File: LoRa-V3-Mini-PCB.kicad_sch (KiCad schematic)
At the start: 23 parts, among them Q1 SI2367DS-T1-GE3, SW1 434331045822, SW2 434331045816, U1 114993121, U2 BR24G1MFVT, U3 SHT40, U4 TSL25911

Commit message: move global components into project library
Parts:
- C1, C10, C11, C2, C3, C5: footprint 1GlobalFootprintsLibrary:C_0603_nominal -> 1projectLibrary:C_0603_nominal
- R1, R2, R3, R4: footprint 1GlobalFootprintsLibrary:R_0603_nominal -> 1projectLibrary:R_0603_nominal
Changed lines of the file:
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@@
 			)
 		)
-		(property "Footprint" "1GlobalFootprintsLibrary:C_0603_nominal"
+		(property "Footprint" "1projectLibrary:C_0603_nominal"
 			(at 35.8648 101.6 0)
 			(effects
@@
 			)
 		)
-		(property "Footprint" "1GlobalFootprintsLibrary:C_0603_nominal"
+		(property "Footprint" "1projectLibrary:C_0603_nominal"
 			(at 55.5752 101.6 0)
 			(effects
@@
 			)
 		)
-		(property "Footprint" "1GlobalFootprintsLibrary:R_0603_nominal"
+		(property "Footprint" "1projectLibrary:R_0603_nominal"
 			(at 96.012 54.61 90)
 			(effects
@@
 			)
 		)
-		(property "Footprint" "1GlobalFootprintsLibrary:R_0603_nominal"
+		(property "Footprint" "1projectLibrary:R_0603_nominal"
 			(at 129.032 73.66 90)
 			(effects
@@
 			)
 		)
-		(property "Footprint" "1GlobalFootprintsLibrary:C_0603_nominal"
+		(property "Footprint" "1projectLibrary:C_0603_nominal"
 			(at 247.3452 62.23 0)
 			(effects
@@
 			)
 		)
-		(property "Footprint" "1GlobalFootprintsLibrary:R_0603_nominal"
+		(property "Footprint" "1projectLibrary:R_0603_nominal"
 			(at 134.112 73.66 90)
 			(effects
@@
 			)
 		)
-		(property "Footprint" "1GlobalFootprintsLibrary:C_0603_nominal"
+		(property "Footprint" "1projectLibrary:C_0603_nominal"
 			(at 46.6852 101.6 0)
 			(effects
@@
 			)
 		)
-		(property "Footprint" "1GlobalFootprintsLibrary:C_0603_nominal"
+		(property "Footprint" "1projectLibrary:C_0603_nominal"
 			(at 253.6952 62.23 0)
 			(effects
@@
 			)
 		)
-		(property "Footprint" "1GlobalFootprintsLibrary:C_0603_nominal"
+		(property "Footprint" "1projectLibrary:C_0603_nominal"
 			(at 265.1252 147.32 0)
 			(effects
@@
 			)
 		)
-		(property "Footprint" "1GlobalFootprintsLibrary:R_0603_nominal"
+		(property "Footprint" "1projectLibrary:R_0603_nominal"
 			(at 139.192 73.66 90)
 			(effects

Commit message: update 3d models / footprints
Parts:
- U1: footprint 1GlobalFootprintsLibrary:LoRa-E5 -> 1projectLibrary:LoRa-E5
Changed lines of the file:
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@@
 			)
 		)
-		(property "Footprint" "1GlobalFootprintsLibrary:LoRa-E5"
+		(property "Footprint" "1projectLibrary:LoRa-E5"
 			(at 233.68 106.68 0)
 			(effects

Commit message: using project lib io global
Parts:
- F1, F2, F3: footprint Fiducial:Fiducial_0.75mm_Mask1.5mm -> Fiducial:Fiducial_0.5mm_Mask1mm
- U3: footprint 1GlobalFootprintsLibrary:SHT4X -> 1projectLibrary:SHT4X
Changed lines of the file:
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@@
 			)
 		)
-		(property "Footprint" "Fiducial:Fiducial_0.75mm_Mask1.5mm"
+		(property "Footprint" "Fiducial:Fiducial_0.5mm_Mask1mm"
 			(at 167.64 180.34 0)
 			(effects
@@
 			)
 		)
-		(property "Footprint" "Fiducial:Fiducial_0.75mm_Mask1.5mm"
+		(property "Footprint" "Fiducial:Fiducial_0.5mm_Mask1mm"
 			(at 167.64 175.26 0)
 			(effects
@@
 			)
 		)
-		(property "Footprint" "Fiducial:Fiducial_0.75mm_Mask1.5mm"
+		(property "Footprint" "Fiducial:Fiducial_0.5mm_Mask1mm"
 			(at 167.64 185.42 0)
 			(effects
@@
 			)
 		)
-		(property "Footprint" "1GlobalFootprintsLibrary:SHT4X"
+		(property "Footprint" "1projectLibrary:SHT4X"
 			(at 68.58 128.27 0)
 			(effects
@@
 			)
 		)
-		(property "Description" "SHT40"
+		(property "Description" "Digital Relative Humidity Temperature Sensor"
 			(at 69.85 110.49 0)
 			(effects

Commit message: update libraries
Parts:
- ANT1: footprint 1GlobalFootprintsLibrary:XDCR_ANT-868-CHP-T -> 1projectLibrary:XDCR_ANT-868-CHP-T
- SW1: manufacturerPartNumber 434331045822 -> 434133025816
- SW2: footprint 1GlobalFootprintsLibrary:4341330258X6 -> 1projectLibrary:4341330258X6; GPN (none) -> NA
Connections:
- net GND: now also SW1.2; no longer SW1.3
- net SWO: now also SW1.3; no longer SW1.2
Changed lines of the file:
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@@
 			)
 		)
-		(property "Datasheet" "https://www.we-online.com/katalog/datasheet/434331045822.pdf"
+		(property "Datasheet" "https://www.we-online.com/components/products/datasheet/434133025816.pdf"
 			(at 205.994 89.662 0)
 			(effects
@@
 			)
 		)
-		(property "Description" "ApplicationButton"
+		(property "Description" "Application buttonswitch"
 			(at 194.31 94.488 0)
 			(effects
@@
 			)
 		)
-		(property "manufacturerPartNumber" "434331045822"
+		(property "manufacturerPartNumber" "434133025816"
 			(at 207.01 87.63 0)
 			(effects
@@
 			)
 		)
-		(property "Footprint" "1GlobalFootprintsLibrary:XDCR_ANT-868-CHP-T"
+		(property "Footprint" "1projectLibrary:XDCR_ANT-868-CHP-T"
 			(at 207.01 132.715 0)
 			(effects
@@
 			)
 		)
-		(property "Footprint" "1GlobalFootprintsLibrary:4341330258X6"
+		(property "Footprint" "1projectLibrary:4341330258X6"
 			(at 254.762 126.746 0)
 			(effects
@@
 			(at 254 143.51 0)
 			(effects
+				(font
+					(size 1.27 1.27)
+				)
+				(hide yes)
+			)
+		)
+		(property "GPN" "NA"
+			(at 254 143.51 0)
+			(effects

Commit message: update application switch
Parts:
- SW1: symbol 1GlobalSymbolsLibrary:Switch_434331045822 -> 1projectLibrary:Switch_434331045822
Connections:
- net GND: now also SW1.3; no longer SW1.2
- net SWO: now also SW1.2; no longer SW1.3
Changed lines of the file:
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@@
 	)
 	(symbol
-		(lib_id "1GlobalSymbolsLibrary:Switch_434331045822")
+		(lib_id "1projectLibrary:Switch_434331045822")
 		(at 207.01 95.25 180)
 		(unit 1)
@@
 			)
 		)
-		(property "Datasheet" "https://www.we-online.com/components/products/datasheet/434133025816.pdf"
+		(property "Datasheet" "https://www.we-online.com/katalog/datasheet/434331045822.pdf"
 			(at 205.994 89.662 0)
 			(effects
@@
 		)
 		(property "Description" "Application buttonswitch"
-			(at 194.31 94.488 0)
+			(at 207.01 74.93 0)
 			(effects
 				(font
 					(size 1.27 1.27)
 				)
+				(hide yes)
 			)
 		)

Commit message: wip
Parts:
- Q1: footprint 1GlobalFootprintsLibrary:SI2367DS-SOT-23 -> 1projectLibrary:SI2367DS-SOT-23; symbol 1GlobalSymbolsLibrary:Si2367DS -> 1projectLibrary:Si2367DS
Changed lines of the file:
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@@
 	)
 	(symbol
-		(lib_id "1GlobalSymbolsLibrary:Si2367DS")
+		(lib_id "1projectLibrary:Si2367DS")
 		(at 90.17 59.69 0)
 		(mirror y)
@@
 			)
 		)
-		(property "Footprint" "1GlobalFootprintsLibrary:SI2367DS-SOT-23"
+		(property "Footprint" "1projectLibrary:SI2367DS-SOT-23"
 			(at 99.568 87.122 0)
 			(effects

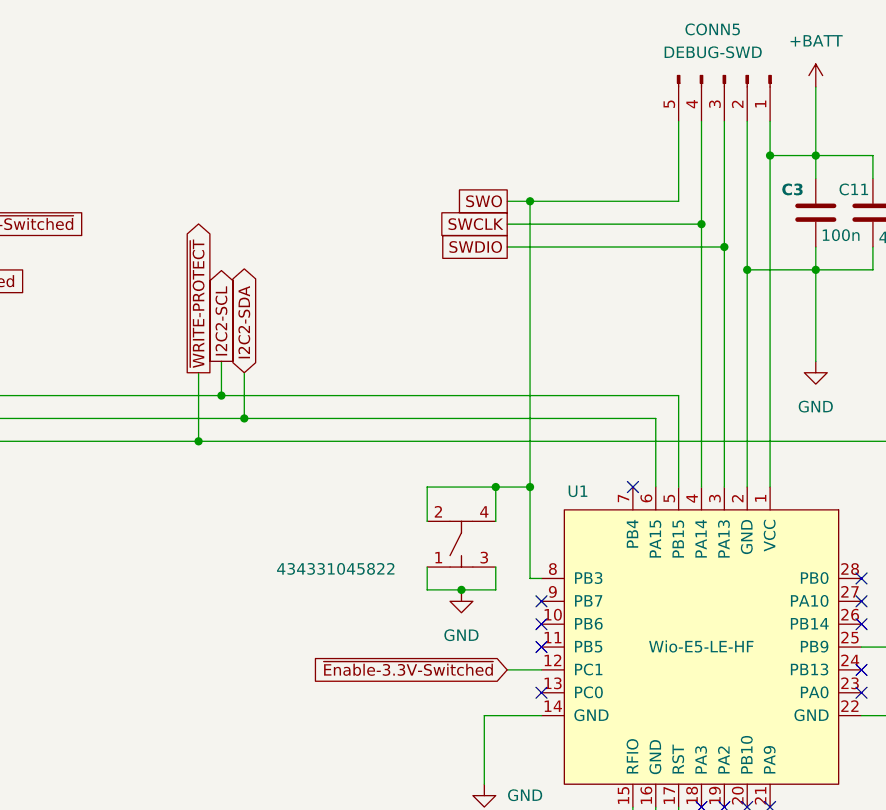
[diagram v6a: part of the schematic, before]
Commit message: upgraded debug connector with UART1TX
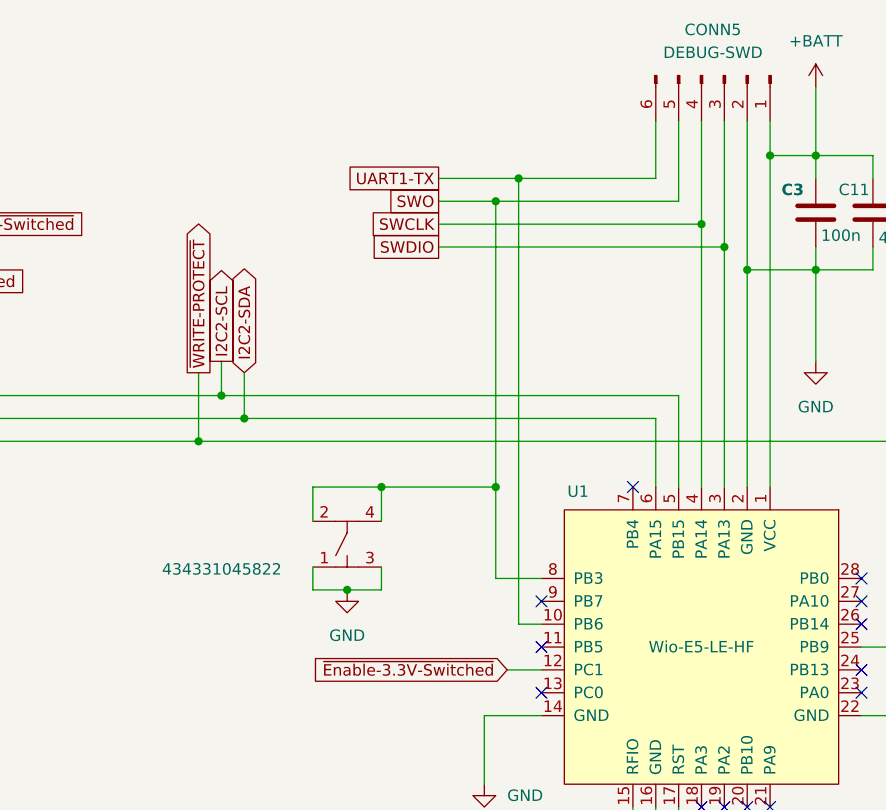
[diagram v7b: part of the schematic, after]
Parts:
- CONN5: footprint 1projectLibrary:PinHeader_1x05_P2.54mm_Vertical -> 1projectLibrary:DebugConnector_1x06_P2.54mm; symbol 1projectLibrary:DebugPortConnector -> 1projectLibrary:DebugConnector-6p
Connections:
- net UART1-TX: now reaches U1.10 (PB6)
- net UART1-TX: now also CONN5.6 (Pin_6)
- no-connect marks 15 -> 14

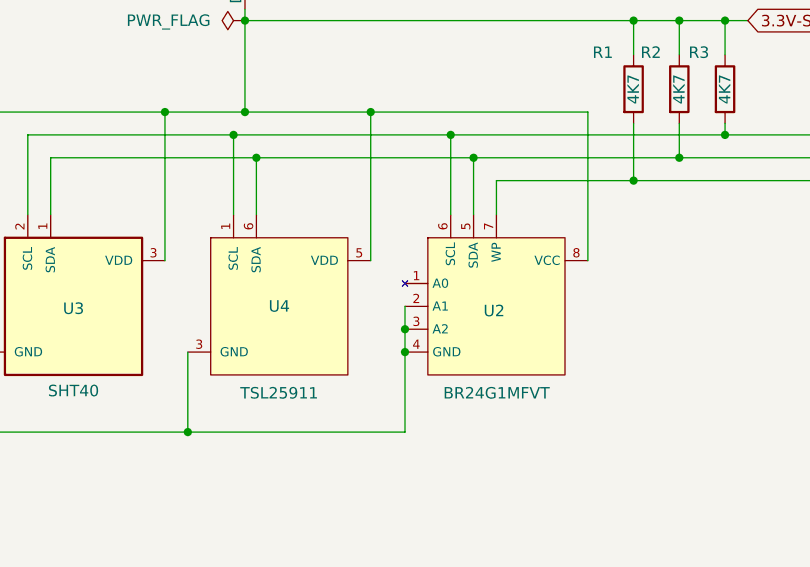
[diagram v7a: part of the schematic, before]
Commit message: fix 3d-models
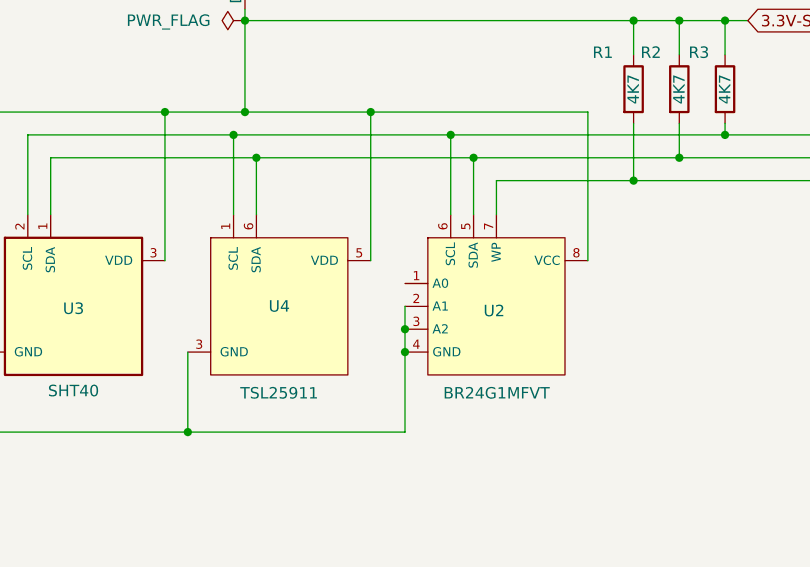
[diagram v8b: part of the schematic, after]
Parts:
- U2: footprint 1GlobalFootprintsLibrary:BR24G1M-TSSOP-B8 -> 1projectLibrary:BR24G1M-TSSOP-B8; symbol 1GlobalSymbolsLibrary:BR24G1MFVT -> 1projectLibrary:BR24G1MFVT
- U4: footprint 1GlobalFootprintsLibrary:TSL2591 -> 1projectLibrary:TSL2591-SON; symbol 1GlobalSymbolsLibrary:TSL2591 -> 1projectLibrary:TSL2591
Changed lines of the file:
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@@
 	)
 	(symbol
-		(lib_id "1GlobalSymbolsLibrary:BR24G1MFVT")
+		(lib_id "1projectLibrary:BR24G1MFVT")
 		(at 115.57 97.79 0)
 		(unit 1)
@@
 			)
 		)
-		(property "Footprint" "1GlobalFootprintsLibrary:BR24G1M-TSSOP-B8"
+		(property "Footprint" "1projectLibrary:BR24G1M-TSSOP-B8"
 			(at 115.57 120.65 0)
 			(effects
@@
 	)
 	(symbol
-		(lib_id "1GlobalSymbolsLibrary:TSL2591")
+		(lib_id "1projectLibrary:TSL2591")
 		(at 91.44 97.79 0)
 		(unit 1)
@@
 			)
 		)
-		(property "Footprint" "1GlobalFootprintsLibrary:TSL2591"
-			(at 91.44 116.84 0)
+		(property "Footprint" "1projectLibrary:TSL2591-SON"
+			(at 96.52 107.95 0)
 			(effects
 				(font
@@
 		)
 		(property "Datasheet" "https://ams.com/documents/20143/36005/TSL2591_DS000338_6-00.pdf/090eb50d-bb18-5b45-4938-9b3672f86b80"
-			(at 91.44 133.35 0)
+			(at 91.186 80.899 0)
 			(effects
 				(font
@@
 		)
 		(property "Description" "Light to Digital Converters Hi-Sensitvty Ambient Light Sensor IC"
-			(at 91.44 113.03 0)
+			(at 89.408 75.311 0)
 			(effects
 				(font
@@
 		)
 		(property "manufacturerName" "ams Osram"
-			(at 91.44 110.49 0)
+			(at 71.12 102.87 0)
 			(effects
 				(font
@@
 		)
 		(property "manufacturerPartNumber" "TSL25911FN"
-			(at 91.44 123.19 0)
-			(effects
-				(font
+			(at 67.183 108.839 0)
+			(effects
+				(font
+					(size 1.27 1.27)
+				)
+				(hide yes)
+			)
+		)
+		(property "octopartURL" ""
+			(at 91.44 97.79 0)
+			(effects
+				(font
